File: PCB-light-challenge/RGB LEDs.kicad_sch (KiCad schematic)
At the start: 1 part

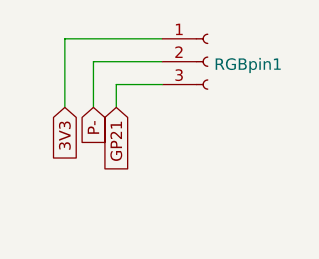
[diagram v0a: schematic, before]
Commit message: 3V3 OUT voor RGB toegevoegd en footprint van connectoren verandert naar JST
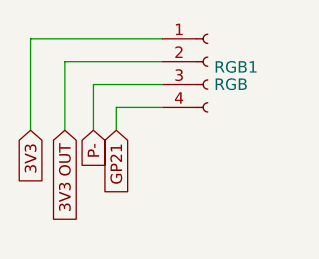
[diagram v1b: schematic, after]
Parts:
- removed RGBpin1: Conn_01x03_Socket, Connector_PinSocket_2.54mm:PinSocket_1x03_P2.54mm_Vertical, symbol Connector:Conn_01x03_Socket
- added RGB1: RGB, Connector_JST:JST_EH_B4B-EH-A_1x04_P2.50mm_Vertical, symbol Connector:Conn_01x04_Socket
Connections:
- net 3V3: now also RGB1.1 (Pin_1)
- net GP21: now also RGB1.4 (Pin_4)
- net P-: now also RGB1.3 (Pin_3)
- new net 3V3 OUT: RGB1.2 (Pin_2)
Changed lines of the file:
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@@
 (kicad_sch (version 20230121) (generator eeschema)
   (paper "A5")
-  (wire (pts (xy 82.55 61.595) (xy 82.55 64.135))
+  (wire (pts (xy 82.55 64.135) (xy 82.55 66.675))
     (stroke (width 0) (type default))
   )
-  (wire (pts (xy 87.63 56.515) (xy 76.835 56.515))
+  (wire (pts (xy 87.63 59.055) (xy 76.835 59.055))
     (stroke (width 0) (type default))
   )
-  (wire (pts (xy 76.835 56.515) (xy 76.835 64.135))
+  (wire (pts (xy 76.835 59.055) (xy 76.835 66.675))
     (stroke (width 0) (type default))
   )
-  (wire (pts (xy 80.01 59.055) (xy 80.01 64.135))
+  (wire (pts (xy 80.01 61.595) (xy 80.01 66.675))
     (stroke (width 0) (type default))
   )
-  (wire (pts (xy 87.63 61.595) (xy 82.55 61.595))
+  (wire (pts (xy 87.63 64.135) (xy 82.55 64.135))
     (stroke (width 0) (type default))
   )
-  (wire (pts (xy 87.63 59.055) (xy 80.01 59.055))
+  (wire (pts (xy 87.63 61.595) (xy 80.01 61.595))
     (stroke (width 0) (type default))
   )
-  (global_label "P-" (shape input) (at 80.01 64.135 270) (fields_autoplaced)
+  (wire (pts (xy 73.025 66.675) (xy 73.025 56.515))
+    (stroke (width 0) (type default))
+  )
+  (wire (pts (xy 73.025 56.515) (xy 87.63 56.515))
+    (stroke (width 0) (type default))
+  )
+  (global_label "P-" (shape input) (at 80.01 66.675 270) (fields_autoplaced)
     (effects (font (size 1.27 1.27)) (justify right))
-    (property "Intersheetrefs" "${INTERSHEET_REFS}" (at 80.01 69.8832 90)
+    (property "Intersheetrefs" "${INTERSHEET_REFS}" (at 80.01 72.4232 90)
       (effects (font (size 1.27 1.27)) (justify right) hide)
     )
   )
-  (global_label "GP21" (shape input) (at 82.55 64.135 270) (fields_autoplaced)
+  (global_label "GP21" (shape input) (at 82.55 66.675 270) (fields_autoplaced)
     (effects (font (size 1.27 1.27)) (justify right))
-    (property "Intersheetrefs" "${INTERSHEET_REFS}" (at 82.55 71.9998 90)
+    (property "Intersheetrefs" "${INTERSHEET_REFS}" (at 82.55 74.5398 90)
       (effects (font (size 1.27 1.27)) (justify right) hide)
     )
   )
-  (global_label "3V3" (shape input) (at 76.835 64.135 270) (fields_autoplaced)
+  (global_label "3V3" (shape input) (at 73.025 66.675 270) (fields_autoplaced)
     (effects (font (size 1.27 1.27)) (justify right))
-    (property "Intersheetrefs" "${INTERSHEET_REFS}" (at 76.835 70.5484 90)
+    (property "Intersheetrefs" "${INTERSHEET_REFS}" (at 73.025 73.0884 90)
       (effects (font (size 1.27 1.27)) (justify right) hide)
     )
   )
-  (symbol (lib_id "Connector:Conn_01x03_Socket") (at 92.71 59.055 0) (unit 1)
+  (global_label "3V3 OUT" (shape input) (at 76.835 66.675 270) (fields_autoplaced)
+    (effects (font (size 1.27 1.27)) (justify right))
+    (property "Intersheetrefs" "${INTERSHEET_REFS}" (at 76.835 77.479 90)
+      (effects (font (size 1.27 1.27)) (justify right) hide)
+    )
+  )
+  (symbol (lib_id "Connector:Conn_01x04_Socket") (at 92.71 59.055 0) (unit 1)
     (in_bom yes) (on_board yes) (dnp no) (fields_autoplaced)
-    (property "Reference" "RGBpin1" (at 93.4212 59.3718 0)
+    (property "Reference" "RGB1" (at 93.4212 59.6813 0)
       (effects (font (size 1.27 1.27)) (justify left))
     )
-    (property "Value" "Conn_01x03_Socket" (at 93.4212 60.3323 0)
-      (effects (font (size 1.27 1.27)) (justify left) hide)
+    (property "Value" "RGB" (at 93.4212 61.6023 0)
+      (effects (font (size 1.27 1.27)) (justify left))
     )
-    (property "Footprint" "Connector_PinSocket_2.54mm:PinSocket_1x03_P2.54mm_Vertical" (at 92.71 59.055 0)
+    (property "Footprint" "Connector_JST:JST_EH_B4B-EH-A_1x04_P2.50mm_Vertical" (at 92.71 59.055 0)
       (effects (font (size 1.27 1.27)) hide)
     )
@@
     (pin "2")
     (pin "3")
+    (pin "4")
     (instances
       (project "PCB-light-challenge"
         (path "/35573e8f-7834-430c-81d2-239f316c7834/1f6a54d7-bb01-4312-8758-614cdc643234"
-          (reference "RGBpin1") (unit 1)
+          (reference "RGB1") (unit 1)
         )
       )
